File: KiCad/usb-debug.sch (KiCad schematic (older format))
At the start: 76 parts, among them IC16 AP22652W6-7, IC7 HD3SS3220, J11 632723300011, Q1 PMV32UP, T6 BSS138APW, T7 BSS138APW

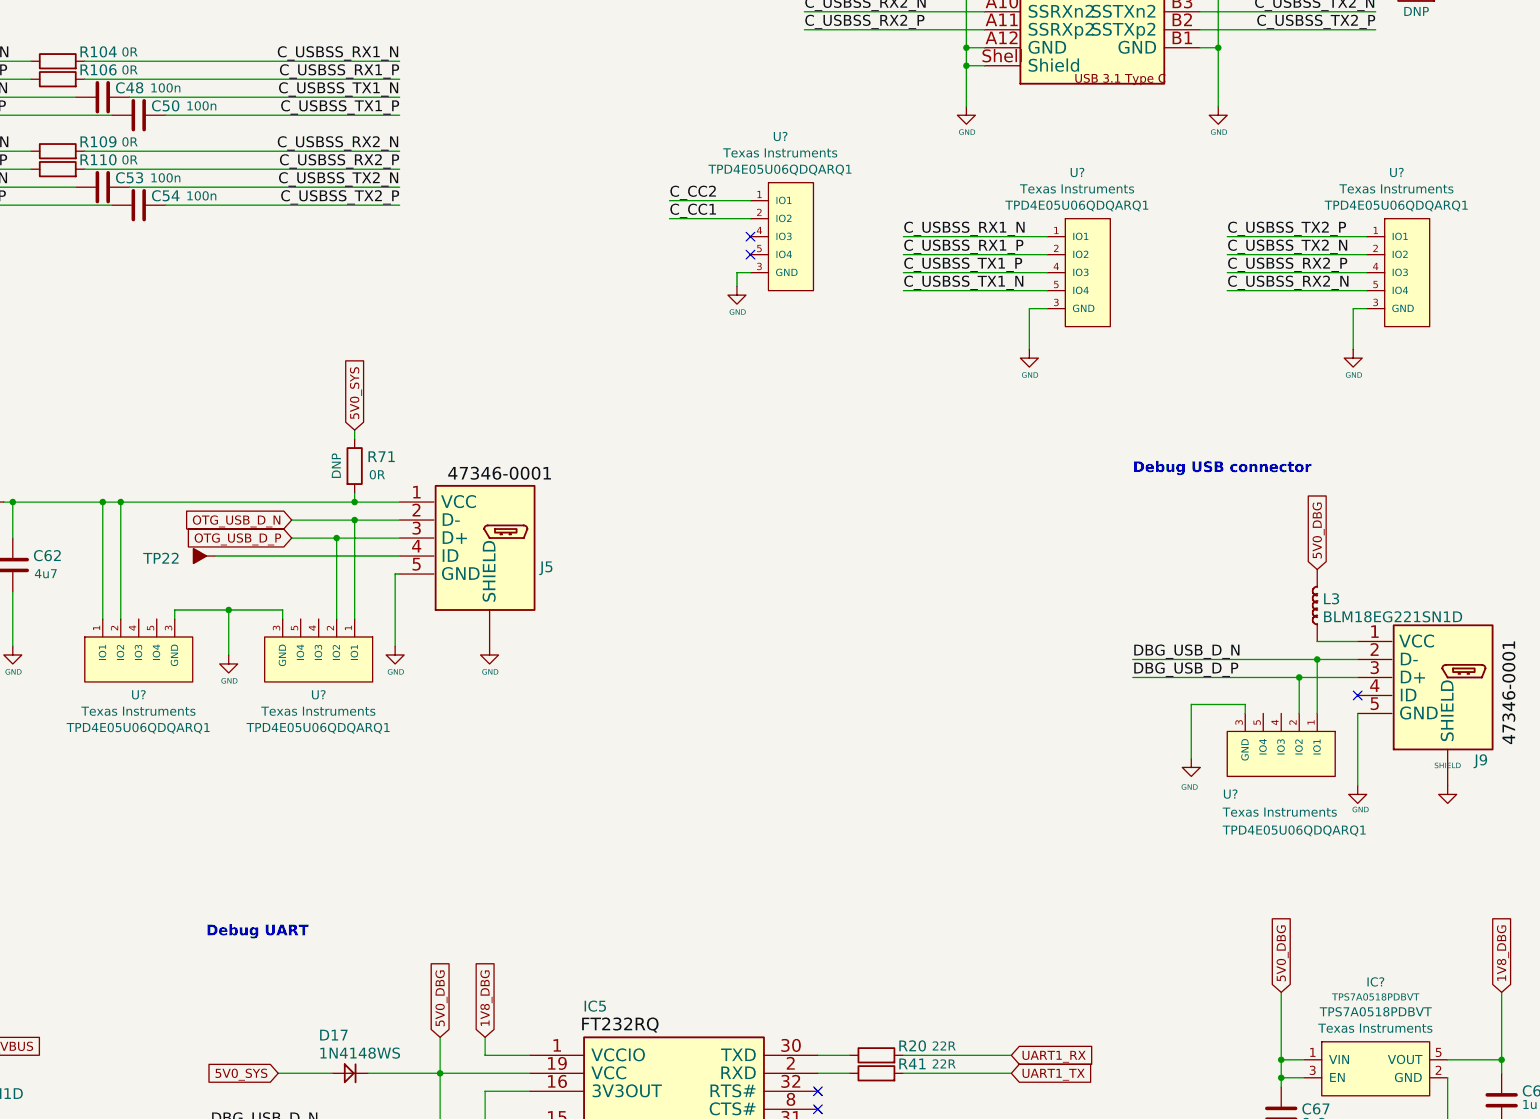
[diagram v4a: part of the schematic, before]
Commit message: Annotate parts
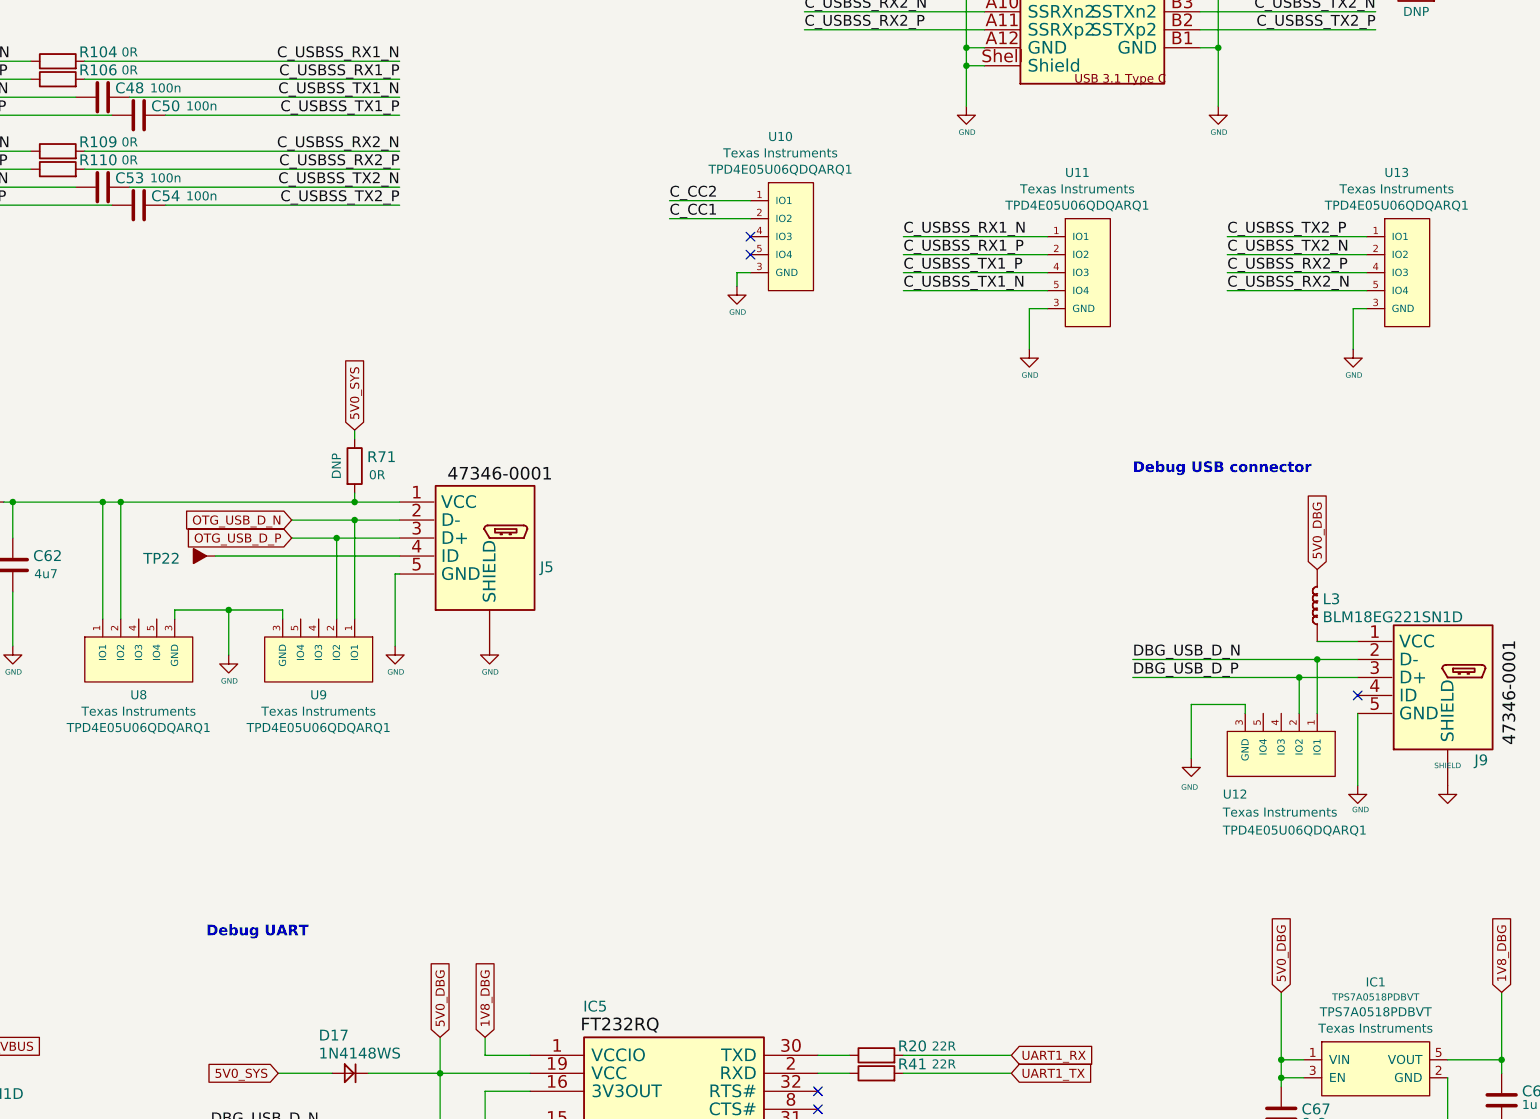
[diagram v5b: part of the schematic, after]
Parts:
- gave numbers to parts that had none: 7
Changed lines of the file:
@@
 $EndComp
 $Comp
-L antmicroTVSDiodes:TPD4E05U06QDQARQ1 U?
+L antmicroTVSDiodes:TPD4E05U06QDQARQ1 U8
 U 1 1 61FB5553
 P 6825 6650
-F 0 "U?" V 7198 6650 50  0000 C CNN
+F 0 "U8" V 7198 6650 50  0000 C CNN
 F 1 "TPD4E05U06QDQARQ1" H 6875 6250 50  0001 L CNN
 F 2 "antmicro-footprints:TPD4E05U06QDQARQ1" H 6875 7100 50  0001 L CNN
@@
 $EndComp
 $Comp
-L antmicroTVSDiodes:TPD4E05U06QDQARQ1 U?
+L antmicroTVSDiodes:TPD4E05U06QDQARQ1 U10
 U 1 1 61FBEC77
 P 10275 4475
-F 0 "U?" H 10392 5030 50  0000 C CNN
+F 0 "U10" H 10392 5030 50  0000 C CNN
 F 1 "TPD4E05U06QDQARQ1" H 10325 4075 50  0001 L CNN
 F 2 "antmicro-footprints:TPD4E05U06QDQARQ1" H 10325 4925 50  0001 L CNN
@@
 $EndComp
 $Comp
-L antmicroTVSDiodes:TPD4E05U06QDQARQ1 U?
+L antmicroTVSDiodes:TPD4E05U06QDQARQ1 U11
 U 1 1 61FE29FF
 P 11925 4675
-F 0 "U?" H 12042 5230 50  0000 C CNN
+F 0 "U11" H 12042 5230 50  0000 C CNN
 F 1 "TPD4E05U06QDQARQ1" H 11975 4275 50  0001 L CNN
 F 2 "antmicro-footprints:TPD4E05U06QDQARQ1" H 11975 5125 50  0001 L CNN
@@
 $EndComp
 $Comp
-L antmicroTVSDiodes:TPD4E05U06QDQARQ1 U?
+L antmicroTVSDiodes:TPD4E05U06QDQARQ1 U13
 U 1 1 61FF8D6D
 P 13700 4675
-F 0 "U?" H 13817 5230 50  0000 C CNN
+F 0 "U13" H 13817 5230 50  0000 C CNN
 F 1 "TPD4E05U06QDQARQ1" H 13750 4275 50  0001 L CNN
 F 2 "antmicro-footprints:TPD4E05U06QDQARQ1" H 13750 5125 50  0001 L CNN
@@
 	12975 7075 12675 7075
 $Comp
-L antmicroTVSDiodes:TPD4E05U06QDQARQ1 U?
+L antmicroTVSDiodes:TPD4E05U06QDQARQ1 U12
 U 1 1 62017093
 P 13175 7175
-F 0 "U?" V 13575 6850 50  0000 L CNN
+F 0 "U12" V 13575 6850 50  0000 L CNN
 F 1 "TPD4E05U06QDQARQ1" H 13225 6775 50  0001 L CNN
 F 2 "antmicro-footprints:TPD4E05U06QDQARQ1" H 13225 7625 50  0001 L CNN
@@
 $EndComp
 $Comp
-L jetson-nano-baseboard:GND #GND_?
+L jetson-nano-baseboard:GND #GND_0107
 U 1 1 622610D8
 P 8775 6750
-F 0 "#GND_?" H 8775 6750 20  0001 C CNN
+F 0 "#GND_0107" H 8775 6750 20  0001 C CNN
 F 1 "GND" H 8779 6605 30  0000 C CNN
 F 2 "" H 8775 6750 70  0001 C CNN
@@
 	6725 5950 6725 6600
 $Comp
-L antmicroTVSDiodes:TPD4E05U06QDQARQ1 U?
+L antmicroTVSDiodes:TPD4E05U06QDQARQ1 U9
 U 1 1 6231E4F6
 P 7825 6650
-F 0 "U?" V 8198 6650 50  0000 C CNN
+F 0 "U9" V 8198 6650 50  0000 C CNN
 F 1 "TPD4E05U06QDQARQ1" H 7875 6250 50  0001 L CNN
 F 2 "antmicro-footprints:TPD4E05U06QDQARQ1" H 7875 7100 50  0001 L CNN
@@
 5V0_DBG
 $Comp
-L antmicroPMICVoltageRegulatorsLinear:TPS7A0518PDBVT IC?
+L antmicroPMICVoltageRegulatorsLinear:TPS7A0518PDBVT IC1
 U 1 1 6241F94F
 P 13700 9100
-F 0 "IC?" H 13700 9581 50  0000 C CNN
+F 0 "IC1" H 13700 9581 50  0000 C CNN
 F 1 "TPS7A0518PDBVT" H 13700 9498 39  0000 C CNN
 F 2 "antmicro-footprints:SOT-23-5" H 13700 8850 50  0001 C CNN

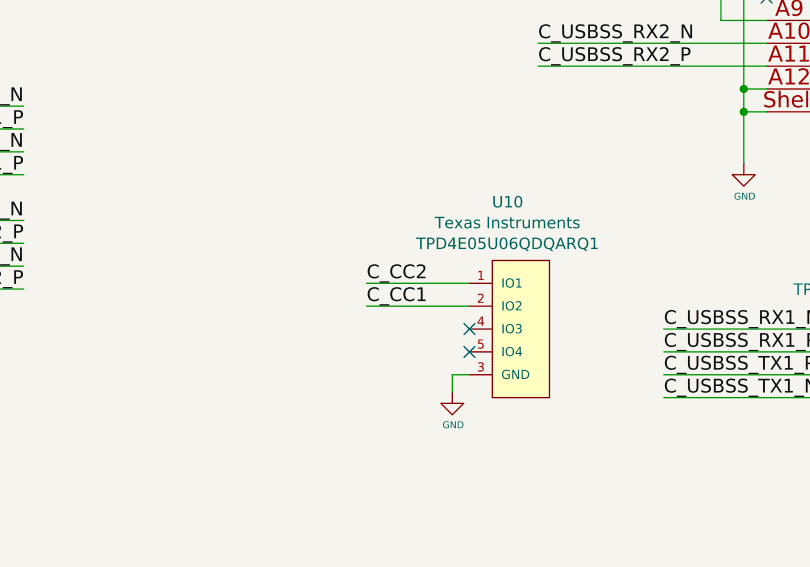
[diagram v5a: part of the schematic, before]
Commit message: Change connections to simplify routing
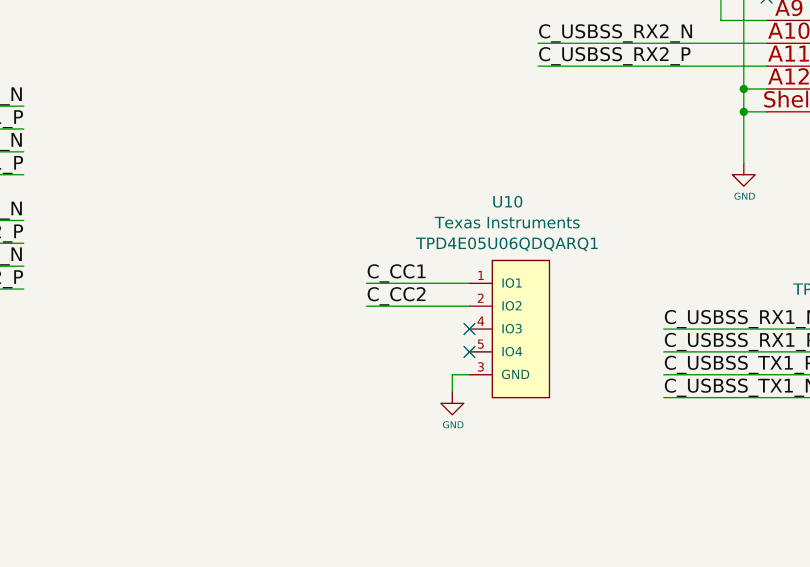
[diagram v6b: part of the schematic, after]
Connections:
- net C_CC1: now also U10.1 (IO1), U10.10 (IO1); no longer U10.2 (IO2), U10.9 (IO2)
- net C_CC2: now also U10.2 (IO2), U10.9 (IO2); no longer U10.1 (IO1), U10.10 (IO1)
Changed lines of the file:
@@
 Text Label 13025 3025 0    60   ~ 0
 C_CC2
+Text Label 9775 4275 0    60   ~ 0
+C_CC1
 Text Label 9775 4375 0    60   ~ 0
-C_CC1
-Text Label 9775 4275 0    60   ~ 0
 C_CC2
 Text Label 9125 5850 2    70   ~ 0

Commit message: Saving changes for later work
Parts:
- removed J5, J9: ~, jetson-nano-baseboard-footprints:CON-Molex-047346-0001, symbol jetson-nano-baseboard:Micro_USB_B
- added J5, J9: 632723300011, jetson-nano-baseboard-footprints:WE_632723300011, symbol jetson-nano-baseboard:WE_632723300011
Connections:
- net labels added: UART2_RX, UART2_TX
- net labels removed: UART1_RX, UART1_TX
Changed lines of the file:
@@
 Text Notes 12350 5800 0    59   ~ 12
 Debug USB connector
-Text Label 14500 7300 1    70   ~ 0
-47346-0001
 Text Label 9280 8911 0    70   ~ 0
 FT232RQ
@@
 L jetson-nano-baseboard:GND #SHIELD01
 U 1 1 5E71036B
-P 14100 7525
-F 0 "#SHIELD01" H 14100 7665 20  0001 C CNN
-F 1 "SHIELD" H 14100 7635 30  0000 C CNN
-F 2 "" H 14100 7525 70  0001 C CNN
-F 3 "" H 14100 7525 70  0001 C CNN
-	1    14100 7525
+P 15825 8400
+F 0 "#SHIELD01" H 15825 8540 20  0001 C CNN
+F 1 "SHIELD" H 15825 8510 30  0000 C CNN
+F 2 "" H 15825 8400 70  0001 C CNN
+F 3 "" H 15825 8400 70  0001 C CNN
+	1    15825 8400
 	1    0    0    -1
 $EndComp
@@
 Wire Wire Line
 	7675 6050 8025 6050
-$Comp
-L jetson-nano-baseboard:Micro_USB_B J5
-U 1 1 5E710320
-P 8775 6250
-F 0 "J5" H 9055 6188 60  0000 L CNN
-F 1 "~" H 8775 6250 50  0001 C CNN
-F 2 "jetson-nano-baseboard-footprints:CON-Molex-047346-0001" H 8775 6250 50  0001 C CNN
-F 3 "" H 8775 6250 50  0001 C CNN
-F 4 "Molex" V 675 -1843 60  0001 C CNN "Manufacturer"
-F 5 "47346-0001" V 675 -1843 60  0001 C CNN "PartSymbol"
-F 6 "473460001" H -31596 -13355 50  0001 C CNN "MPN"
-	1    8775 6250
-	1    0    0    -1
-$EndComp
 Wire Wire Line
 	8275 6150 7925 6150
@@
 Wire Wire Line
 	5375 8975 5775 8975
-$Comp
-L jetson-nano-baseboard:Micro_USB_B J9
-U 1 1 5E710332
-P 14100 7025
-F 0 "J9" H 14325 6700 60  0000 R TNN
-F 1 "~" H 14100 7025 50  0001 C CNN
-F 2 "jetson-nano-baseboard-footprints:CON-Molex-047346-0001" H 14100 7025 50  0001 C CNN
-F 3 "" H 14100 7025 50  0001 C CNN
-F 4 "Molex" V 900 6732 60  0001 C CNN "Manufacturer"
-F 5 "47346-0001" V 900 6732 60  0001 C CNN "PartSymbol"
-F 6 "473460001" H -24860 -20787 50  0001 C CNN "MPN"
-	1    14100 7025
-	1    0    0    -1
-$EndComp
 Wire Wire Line
 	13600 7125 13600 7525
@@
 USBSS_RX6_N
 Text GLabel 11675 9025 2    50   Input ~ 0
-UART1_RX
+UART2_RX
 Text GLabel 11675 9125 2    50   Input ~ 0
-UART1_TX
+UART2_TX
 $Comp
 L jetson-nano-baseboard:R_0R_0402 R103
@@
 	1    0    0    -1
 $EndComp
+$Comp
+L jetson-nano-baseboard:WE_632723300011 J5
+U 1 1 6283AAB4
+P 9550 5675
+F 0 "J5" H 9554 5830 60  0000 L BNN
+F 1 "632723300011" H 9554 5705 60  0000 L BNN
+F 2 "jetson-nano-baseboard-footprints:WE_632723300011" H 9550 5675 60  0001 C CNN
+F 3 "" H 9550 5675 60  0001 C CNN
+F 4 "Wurth Elektronik" V -1150 1082 60  0001 C CNN "Manufacturer"
+F 5 "632723300011" H -33421 -10430 50  0001 C CNN "MPN"
+	1    9550 5675
+	1    0    0    -1
+$EndComp
+$Comp
+L jetson-nano-baseboard:WE_632723300011 J9
+U 1 1 6285123F
+P 14675 6300
+F 0 "J9" H 14679 6455 60  0000 L BNN
+F 1 "632723300011" H 14679 6330 60  0000 L BNN
+F 2 "jetson-nano-baseboard-footprints:WE_632723300011" H 14675 6300 60  0001 C CNN
+F 3 "" H 14675 6300 60  0001 C CNN
+F 4 "Wurth Elektronik" V 3975 1707 60  0001 C CNN "Manufacturer"
+F 5 "632723300011" H -28296 -9805 50  0001 C CNN "MPN"
+	1    14675 6300
+	1    0    0    -1
+$EndComp
